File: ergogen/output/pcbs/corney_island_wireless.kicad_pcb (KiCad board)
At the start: 2 copper layers, 117.7 x 91.7 mm, 66 parts

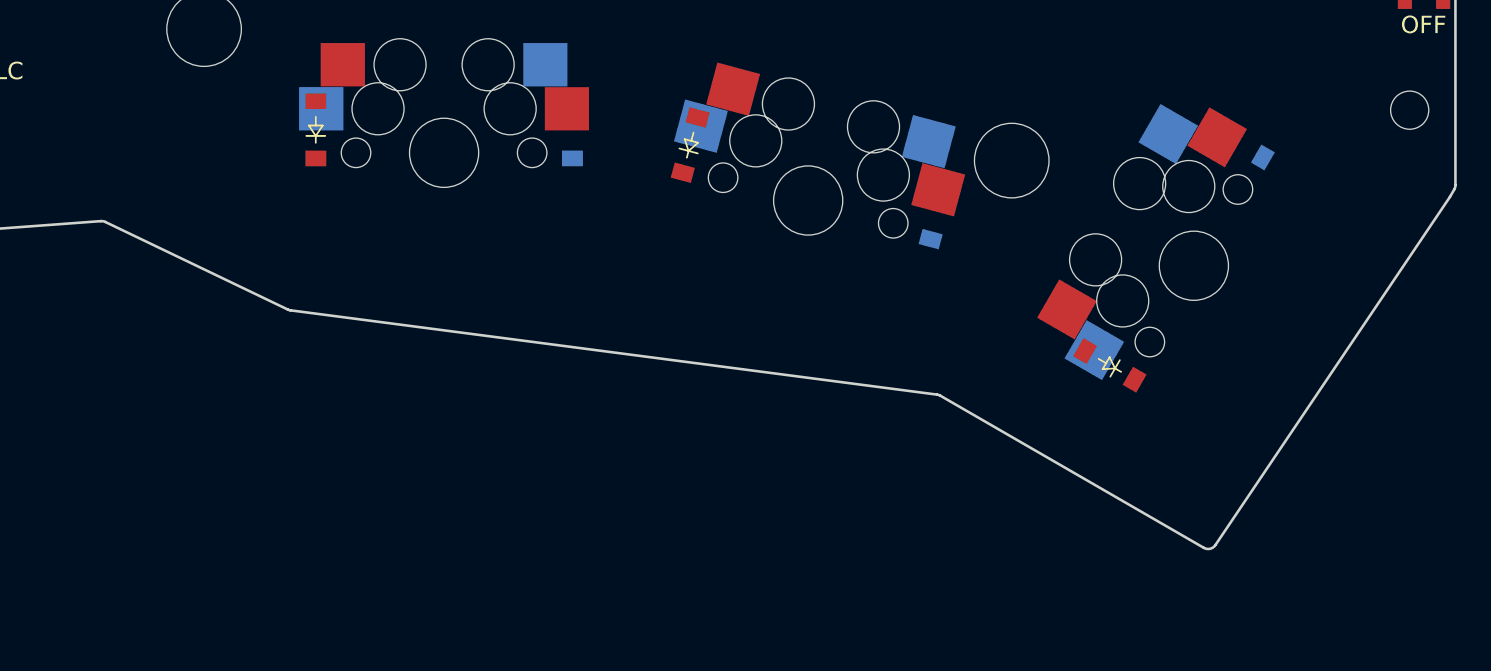
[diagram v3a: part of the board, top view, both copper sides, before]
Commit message: Changed thumb key back to 1u
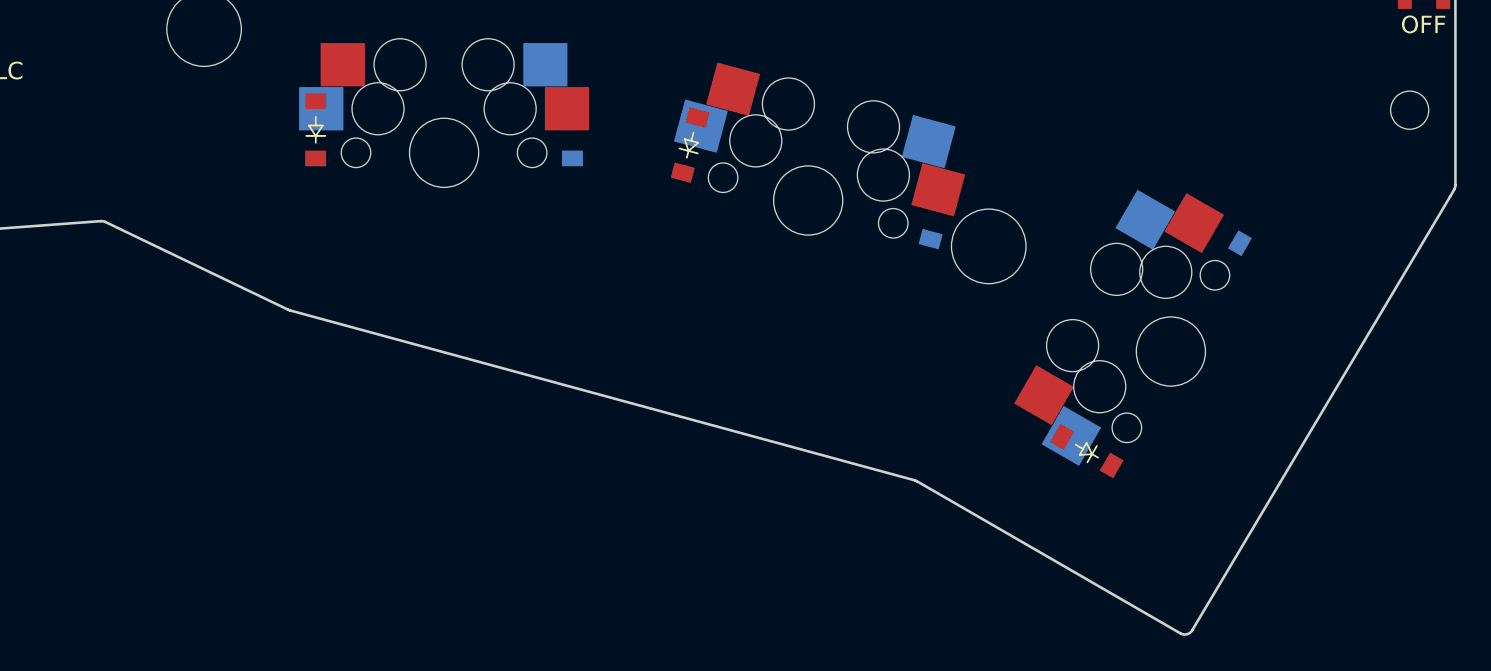
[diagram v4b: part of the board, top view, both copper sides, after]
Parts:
- moved D18 5.12 mm to (190.9, 107.9)
- moved D36 5.12 mm to (183.5, 120.7)
- moved MH7 5.12 mm to (177.8, 108.9)
- moved S18 5.12 mm to (188.3, 114.9)
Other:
- board size 117.7 x 91.7 mm -> 117.7 x 96.7 mm
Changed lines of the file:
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@@
   )
   (module "ceoloide:mounting_hole_npth" (layer F.Cu)
-      (at 179.1254966 103.9282479 60)
+      (at 177.7998255 108.87572 60)
       (fp_text reference "MH7" (at 0 2.55 60) (layer F.SilkS) hide (effects (font (size 1 1) (thickness 0.15))))
       (pad "" np_thru_hole circle (at 0 0 60) (size 4.3 4.3) (drill 4.3) (layers *.Cu *.Mask))
@@
         )
       (module MX (layer F.Cu)
-      (at 189.6312508 109.9937479 60)
+      (at 188.3055797 114.94122 60)
       (fp_text reference "S18" (at 0 0) (layer F.SilkS) hide (effects (font (size 1.27 1.27) (thickness 0.15))))
       (fp_text value "" (at 0 0) (layer F.SilkS) hide (effects (font (size 1.27 1.27) (thickness 0.15))))
@@
         )
         (module "ceoloide:diode_tht_sod123" (layer B.Cu)
-            (at 192.1837671 102.9226599 150)
+            (at 190.85809600000002 107.870132 150)
             (fp_text reference "D18" (at 0 0 150) (layer B.SilkS) hide (effects (font (size 1.27 1.27) (thickness 0.15))))
             (fp_line (start 0.25 0) (end 0.75 0) (layer B.SilkS) (width 0.1))
@@
         )
         (module "ceoloide:diode_tht_sod123" (layer F.Cu)
-            (at 184.7837671 115.7398359 150)
+            (at 183.458096 120.687308 150)
             (fp_text reference "D36" (at 0 0 150) (layer F.SilkS) hide (effects (font (size 1.27 1.27) (thickness 0.15))))
             (fp_line (start 0.25 0) (end 0.75 0) (layer F.SilkS) (width 0.1))
@@
 (gr_line (start 165.47394415076104 43.03997791277865) (end 183.45917122939375 42.77019950801905) (layer Edge.Cuts) (stroke (width 0.15) (type default)))
 (gr_line (start 183.96667038015485 43.26992130873259) (end 183.96722317371228 44.51481240004068) (layer Edge.Cuts) (stroke (width 0.15) (type default)))
-(gr_line (start 204.4024451 106.02118640000002) (end 190.86864454351888 126.1091037392597) (layer Edge.Cuts) (stroke (width 0.15) (type default)))
-(gr_line (start 190.20397584351886 126.26274233925967) (end 175.00808706223268 117.489391839137) (layer Edge.Cuts) (stroke (width 0.15) (type default)))
-(gr_line (start 174.82271206223268 117.42659853913699) (end 137.52391425873893 112.56494858875345) (layer Edge.Cuts) (stroke (width 0.15) (type default)))
-(gr_line (start 137.3721942392345 112.5199139793924) (end 126.84466306000907 107.46728833906016) (layer Edge.Cuts) (stroke (width 0.15) (type default)))
+(gr_line (start 204.4024451 106.02118640000002) (end 189.53461200661962 131.01926453205544) (layer Edge.Cuts) (stroke (width 0.15) (type default)))
+(gr_line (start 188.8548751066196 131.19668733205546) (end 173.65217521437296 122.41940443517656) (layer Edge.Cuts) (stroke (width 0.15) (type default)))
+(gr_line (start 173.533396814373 122.36994343517657) (end 137.48845271108377 112.56655937095499) (layer Edge.Cuts) (stroke (width 0.15) (type default)))
+(gr_line (start 137.40332929157933 112.53485706159397) (end 126.84466306000907 107.46728833906015) (layer Edge.Cuts) (stroke (width 0.15) (type default)))
 (gr_line (start 126.59146074050466 107.41942002969911) (end 92.41319770323031 109.94573156980263) (layer Edge.Cuts) (stroke (width 0.15) (type default)))
 (gr_line (start 184.46722317371226 45.01459040000001) (end 204.2174451 45.01459040000001) (layer Edge.Cuts) (stroke (width 0.15) (type default)))
@@
 (gr_arc (start 204.7174451 45.51459040000001) (mid 204.5709985 45.16103700000001) (end 204.2174451 45.01459040000001) (layer Edge.Cuts) (stroke (width 0.15) (type default)))
 (gr_arc (start 204.6504578 105.59161580612954) (mid 204.70040799999998 105.47102530612953) (end 204.7174451 105.34161580612954) (layer Edge.Cuts) (stroke (width 0.15) (type default)))
-(gr_arc (start 190.2039758435189 126.26274233925966) (mid 190.56658204351888 126.31688453925965) (end 190.86864454351888 126.10910373925965) (layer Edge.Cuts) (stroke (width 0.15) (type default)))
-(gr_arc (start 175.00808706223268 117.489391839137) (mid 174.91850206223268 117.448836139137) (end 174.82271206223268 117.426598539137) (layer Edge.Cuts) (stroke (width 0.15) (type default)))
-(gr_arc (start 137.37219425873894 112.51991398875344) (mid 137.44626115873893 112.54847228875344) (end 137.52391425873893 112.56494858875345) (layer Edge.Cuts) (stroke (width 0.15) (type default)))
+(gr_arc (start 188.8548751066196 131.1966873320555) (mid 189.2311528066196 131.2474658320555) (end 189.5346120066196 131.01926453205547) (layer Edge.Cuts) (stroke (width 0.15) (type default)))
+(gr_arc (start 173.65217521437296 122.41940443517656) (mid 173.59438361437296 122.39083733517657) (end 173.53339681437296 122.36994343517657) (layer Edge.Cuts) (stroke (width 0.15) (type default)))
+(gr_arc (start 137.40332931108378 112.534857070955) (mid 137.44516961108377 112.55264527095501) (end 137.48845271108377 112.566559370955) (layer Edge.Cuts) (stroke (width 0.15) (type default)))
 (gr_arc (start 126.84466304050464 107.46728832969912) (mid 126.72119864050464 107.42676222969911) (end 126.59146074050464 107.41942002969911) (layer Edge.Cuts) (stroke (width 0.15) (type default)))
 (gr_arc (start 91.8782446032303 109.49068746980264) (mid 92.0523782032303 109.82794416980263) (end 92.4131977032303 109.94573156980263) (layer Edge.Cuts) (stroke (width 0.15) (type default)))

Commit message: Changed thumb splay
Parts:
- moved MH7 31.9 mm to (206.5, 122.9), turned to -45 degrees
- moved D18 30.9 mm to (204.1, 135.8), turned to 45 degrees
- moved S18 19.1 mm to (197.9, 131.5), turned to -45 degrees
- moved D17 18.0 mm to (187.0, 120.2), turned to 60 degrees
- moved S17 17.0 mm to (180.0, 117.7), turned to -30 degrees
- moved D35 16.8 mm to (174.2, 112.8), turned to 60 degrees
- moved MH6 16.5 mm to (148.9, 99.1), turned to -15 degrees
- moved D16 16.2 mm to (167.9, 110.2), turned to 75 degrees
- moved S16 15.3 mm to (160.4, 109.6), turned to -15 degrees
- moved D34 15.2 mm to (153.6, 106.4), turned to 75 degrees
- moved D36 11.2 mm to (193.6, 125.3), turned to 45 degrees
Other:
- board size 117.7 x 96.7 mm -> 124.2 x 110.1 mm

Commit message: Moved screws back onto board
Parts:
- moved MH3 24.2 mm to (107.4, 57.9), turned to 0 degrees
- moved MH4 23.6 mm to (108.4, 76.9), turned to 0 degrees
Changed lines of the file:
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@@
   )
   (module "ceoloide:mounting_hole_npth" (layer F.Cu)
-      (at 88.05221169999999 72.4364306 5)
-      (fp_text reference "MH3" (at 0 2.55 5) (layer F.SilkS) hide (effects (font (size 1 1) (thickness 0.15))))
-      (pad "" np_thru_hole circle (at 0 0 5) (size 4.3 4.3) (drill 4.3) (layers *.Cu *.Mask))
+      (at 107.384445 57.919590400000004 0)
+      (fp_text reference "MH3" (at 0 2.55 0) (layer F.SilkS) hide (effects (font (size 1 1) (thickness 0.15))))
+      (pad "" np_thru_hole circle (at 0 0 0) (size 4.3 4.3) (drill 4.3) (layers *.Cu *.Mask))
   )
   (module "ceoloide:mounting_hole_npth" (layer F.Cu)
-      (at 89.70817079999999 91.3641299 5)
-      (fp_text reference "MH4" (at 0 2.55 5) (layer F.SilkS) hide (effects (font (size 1 1) (thickness 0.15))))
-      (pad "" np_thru_hole circle (at 0 0 5) (size 4.3 4.3) (drill 4.3) (layers *.Cu *.Mask))
+      (at 108.384445 76.9195904 0)
+      (fp_text reference "MH4" (at 0 2.55 0) (layer F.SilkS) hide (effects (font (size 1 1) (thickness 0.15))))
+      (pad "" np_thru_hole circle (at 0 0 0) (size 4.3 4.3) (drill 4.3) (layers *.Cu *.Mask))
   )
   (module "ceoloide:mounting_hole_npth" (layer F.Cu)

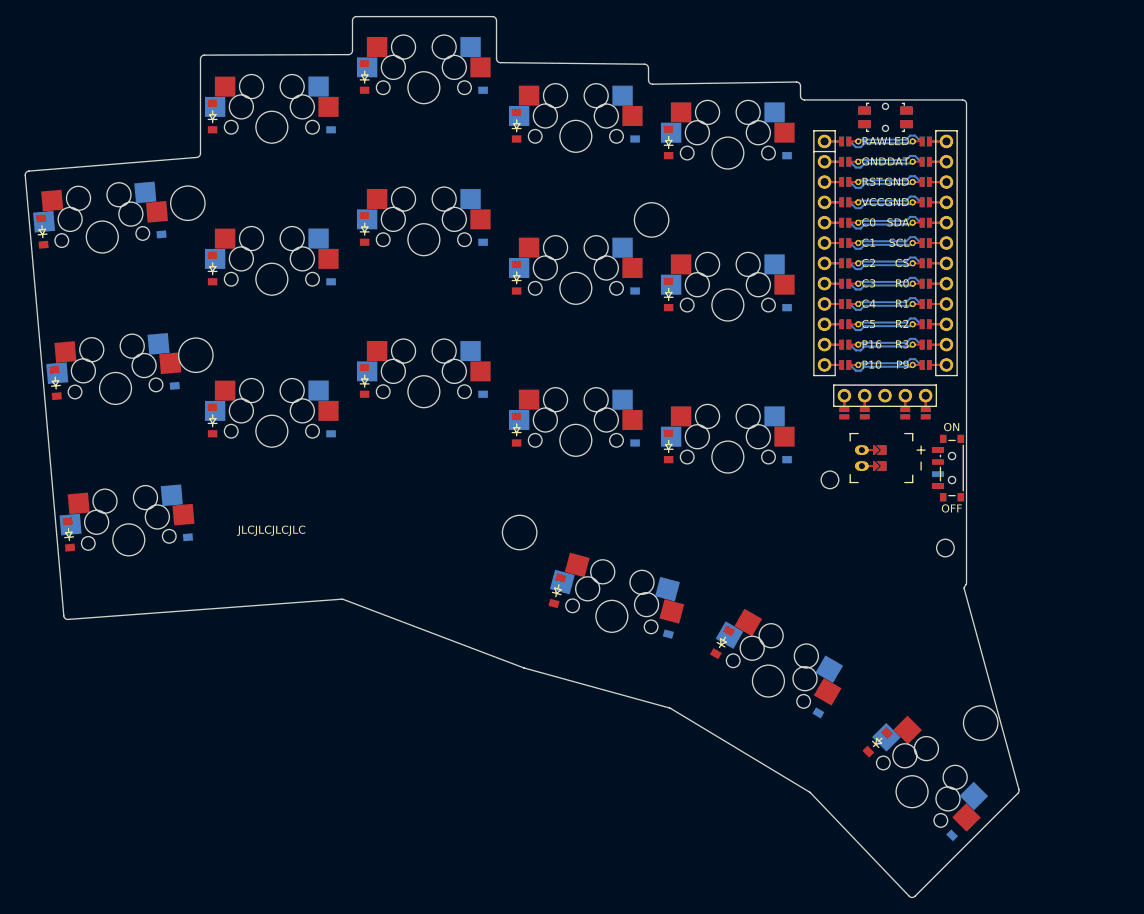
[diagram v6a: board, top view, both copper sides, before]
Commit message: Moved screws around a bit
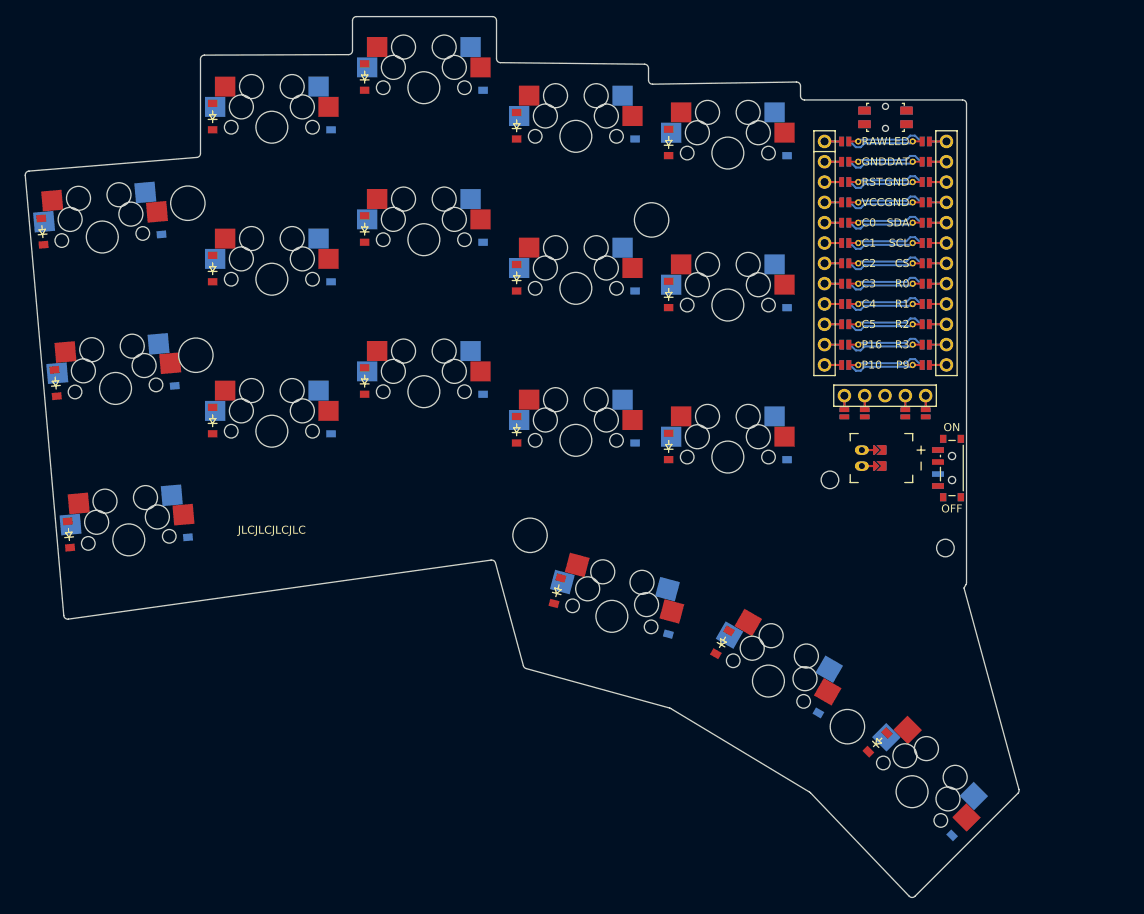
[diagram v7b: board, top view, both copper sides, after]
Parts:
- moved MH7 16.7 mm to (189.8, 123.4), turned to -30 degrees
- moved MH6 1.34 mm to (150.2, 99.4)
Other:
- outline, holes or cut-outs redrawn
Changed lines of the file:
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@@
   )
   (module "ceoloide:mounting_hole_npth" (layer F.Cu)
-      (at 148.8598077 99.0848776 -15)
+      (at 150.1570461 99.4324716 -15)
       (fp_text reference "MH6" (at 0 2.55 -15) (layer F.SilkS) hide (effects (font (size 1 1) (thickness 0.15))))
       (pad "" np_thru_hole circle (at 0 0 -15) (size 4.3 4.3) (drill 4.3) (layers *.Cu *.Mask))
   )
   (module "ceoloide:mounting_hole_npth" (layer F.Cu)
-      (at 206.488576 122.90275019999999 -45)
-      (fp_text reference "MH7" (at 0 2.55 -45) (layer F.SilkS) hide (effects (font (size 1 1) (thickness 0.15))))
-      (pad "" np_thru_hole circle (at 0 0 -45) (size 4.3 4.3) (drill 4.3) (layers *.Cu *.Mask))
+      (at 189.8298246 123.3510864 -30)
+      (fp_text reference "MH7" (at 0 2.55 -30) (layer F.SilkS) hide (effects (font (size 1 1) (thickness 0.15))))
+      (pad "" np_thru_hole circle (at 0 0 -30) (size 4.3 4.3) (drill 4.3) (layers *.Cu *.Mask))
   )
       (module MX (layer F.Cu)
@@
         (segment (start 193.434 88.775) (end 191.634 88.775) (width 0.25) (layer "F.Cu") (net 74))
         (segment (start 193.434 88.775) (end 191.634 88.775) (width 0.25) (layer "B.Cu") (net 74))
-  (gr_line (start 91.87824460323029 109.49068746980254) (end 87.06061104775414 54.447423555018986) (layer Edge.Cuts) (stroke (width 0.15) (type default)))
+  (gr_line (start 91.87535728883249 109.45769882370212) (end 87.06061104775414 54.447423555018986) (layer Edge.Cuts) (stroke (width 0.15) (type default)))
 (gr_line (start 87.51811429808367 53.90547845906503) (end 108.50503754967045 52.19601094528491) (layer Edge.Cuts) (stroke (width 0.15) (type default)))
 (gr_line (start 108.964445 51.69766144933076) (end 108.964445 39.90788282277217) (layer Edge.Cuts) (stroke (width 0.15) (type default)))
@@
 (gr_line (start 197.5573001306715 144.5456552181502) (end 185.2184018103768 131.6245719172887) (layer Edge.Cuts) (stroke (width 0.15) (type default)))
 (gr_line (start 185.11474537091743 131.54156036435938) (end 167.73632242747522 121.07577102297391) (layer Edge.Cuts) (stroke (width 0.15) (type default)))
-(gr_line (start 167.61101352447525 121.02201021014679) (end 149.42297909295323 116.01776895205687) (layer Edge.Cuts) (stroke (width 0.15) (type default)))
-(gr_line (start 149.37827902664569 116.003177061327) (end 126.82809141312292 107.44890800214452) (layer Edge.Cuts) (stroke (width 0.15) (type default)))
-(gr_line (start 126.61389341312291 107.4177619021445) (end 92.41319770323031 109.94573156980263) (layer Edge.Cuts) (stroke (width 0.15) (type default)))
+(gr_line (start 167.61101352447525 121.02201021014679) (end 149.67542832928424 116.0872276331902) (layer Edge.Cuts) (stroke (width 0.15) (type default)))
+(gr_line (start 149.32552987561743 115.73612318902917) (end 145.83984366392013 102.89472334271511) (layer Edge.Cuts) (stroke (width 0.15) (type default)))
+(gr_line (start 145.28816068340882 102.53050838832783) (end 92.4425969819845 109.90929922465821) (layer Edge.Cuts) (stroke (width 0.15) (type default)))
 (gr_line (start 184.46722317371226 45.01459040000001) (end 204.2174451 45.01459040000001) (layer Edge.Cuts) (stroke (width 0.15) (type default)))
 (gr_line (start 204.7174451 45.51459040000001) (end 204.7174451 105.34161580612954) (layer Edge.Cuts) (stroke (width 0.15) (type default)))
@@
 (gr_arc (start 185.21840173422504 131.62457194226215) (mid 185.16934173422504 131.57960944226215) (end 185.11474533422503 131.54156034226216) (layer Edge.Cuts) (stroke (width 0.15) (type default)))
 (gr_arc (start 167.7363223907828 121.07577100087666) (mid 167.6755091907828 121.04459890087666) (end 167.6110134907828 121.02201020087666) (layer Edge.Cuts) (stroke (width 0.15) (type default)))
-(gr_arc (start 149.37827902664569 116.003177061327) (mid 149.4004574266457 116.010998761327) (end 149.42297912664569 116.017768961327) (layer Edge.Cuts) (stroke (width 0.15) (type default)))
-(gr_arc (start 126.8280914131229 107.4489080021445) (mid 126.72269801312291 107.4216051021445) (end 126.61389341312291 107.4177619021445) (layer Edge.Cuts) (stroke (width 0.15) (type default)))
-(gr_arc (start 91.8782446032303 109.49068746980264) (mid 92.0523782032303 109.82794416980263) (end 92.4131977032303 109.94573156980263) (layer Edge.Cuts) (stroke (width 0.15) (type default)))
+(gr_arc (start 149.32552986297674 115.73612314246033) (mid 149.45390776297674 115.95808674246032) (end 149.67542826297674 116.08722764246032) (layer Edge.Cuts) (stroke (width 0.15) (type default)))
+(gr_arc (start 145.83984367656083 102.89472338928387) (mid 145.63278067656083 102.60843598928388) (end 145.28816067656084 102.53050828928387) (layer Edge.Cuts) (stroke (width 0.15) (type default)))
+(gr_arc (start 91.87535728883246 109.45769882370203) (mid 92.06202788883246 109.80527372370203) (end 92.44259698883246 109.90929922370204) (layer Edge.Cuts) (stroke (width 0.15) (type default)))
 )

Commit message: Tweak shape
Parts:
- removed MH6, MH7: , ceoloide:mounting_hole_npth
- moved MH2 96.7 mm to (108.4, 76.9)
- moved MH1 87.4 mm to (107.4, 57.9)
- moved MH5 67.9 mm to (189.8, 123.4), turned to -30 degrees
- moved MH3 58.0 mm to (165.4, 60.0)
- moved MH4 47.5 mm to (150.2, 99.4), turned to -15 degrees
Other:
- board size 124.2 x 110.1 mm -> 124.1 x 110.1 mm
